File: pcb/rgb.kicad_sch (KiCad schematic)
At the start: 40 parts, among them J1 2.54-2*8P, J3 B4PS-VH, J4 TYPE-C-31-M-12, J5 TF-01A, J7 B4PS-VH, SW1 MS-22C01-G010, U4 EVQQ2, U5 ESP32-WROOM-32E, U7 CH340C, U8 SPX3819M5-L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

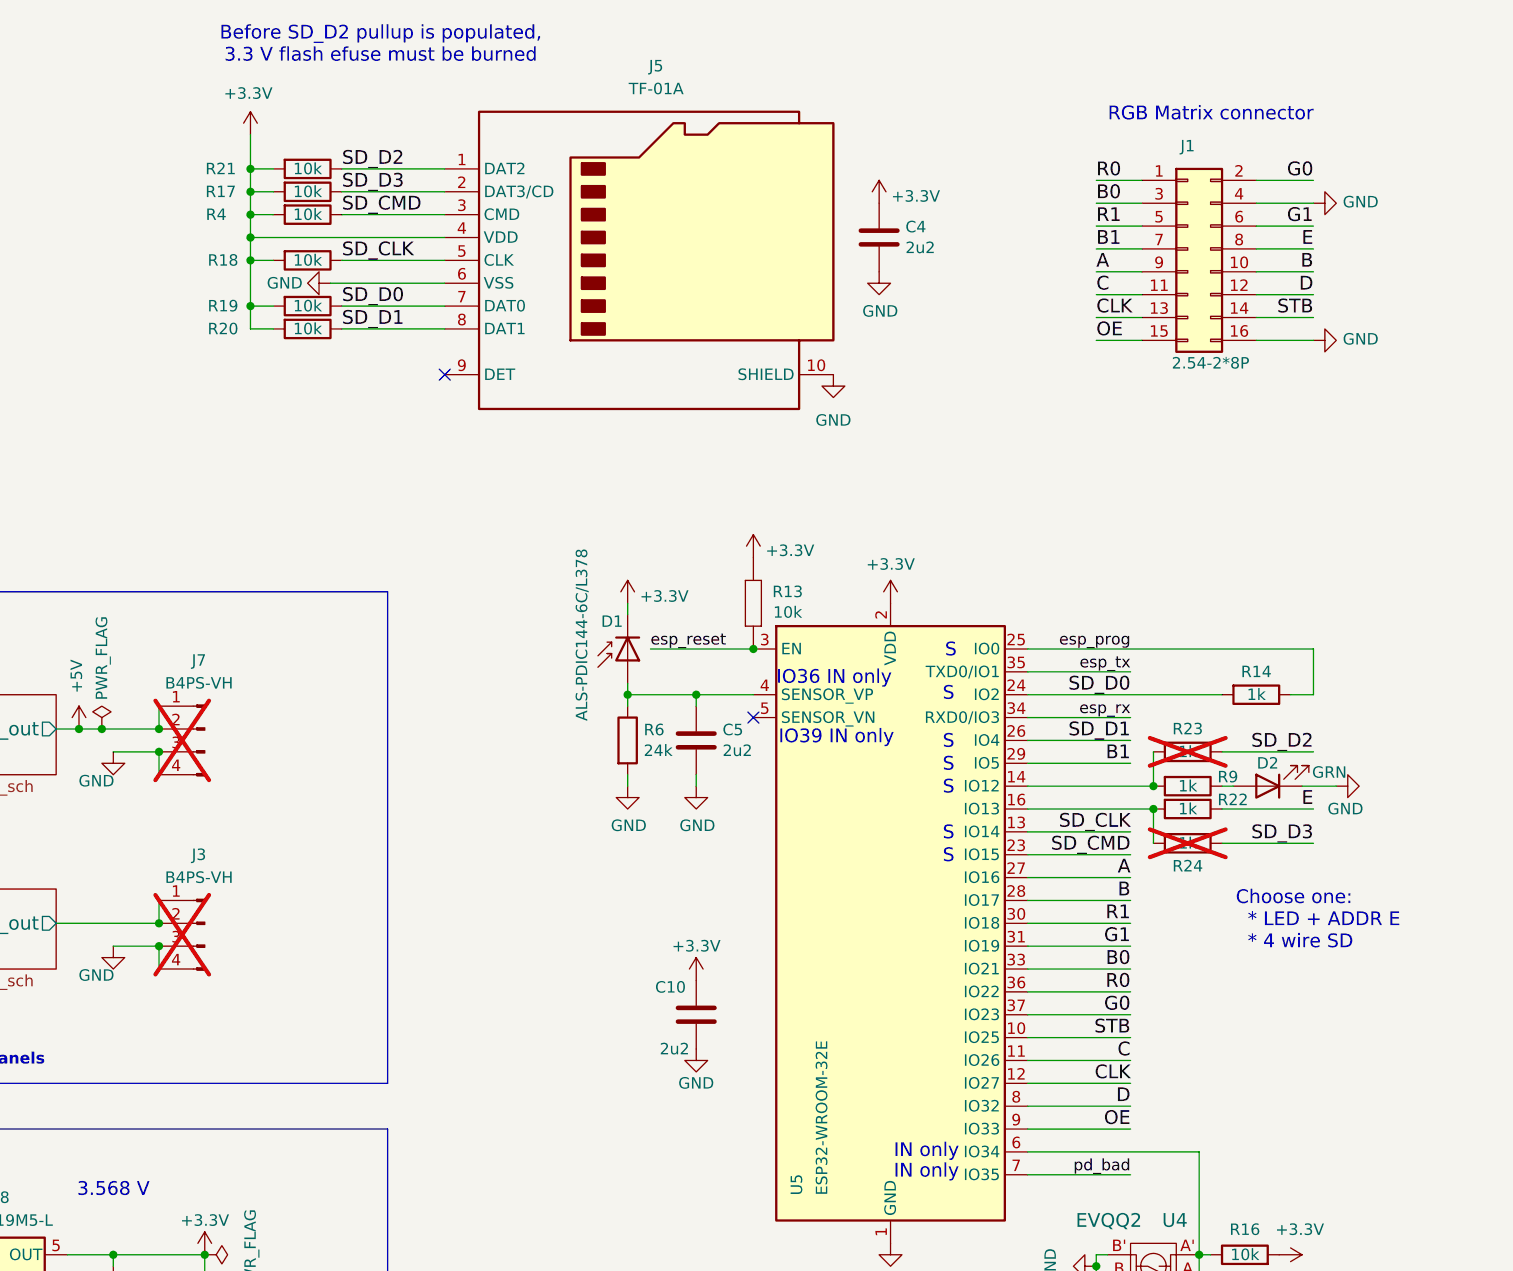
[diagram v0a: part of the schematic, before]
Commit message: sch: move comment
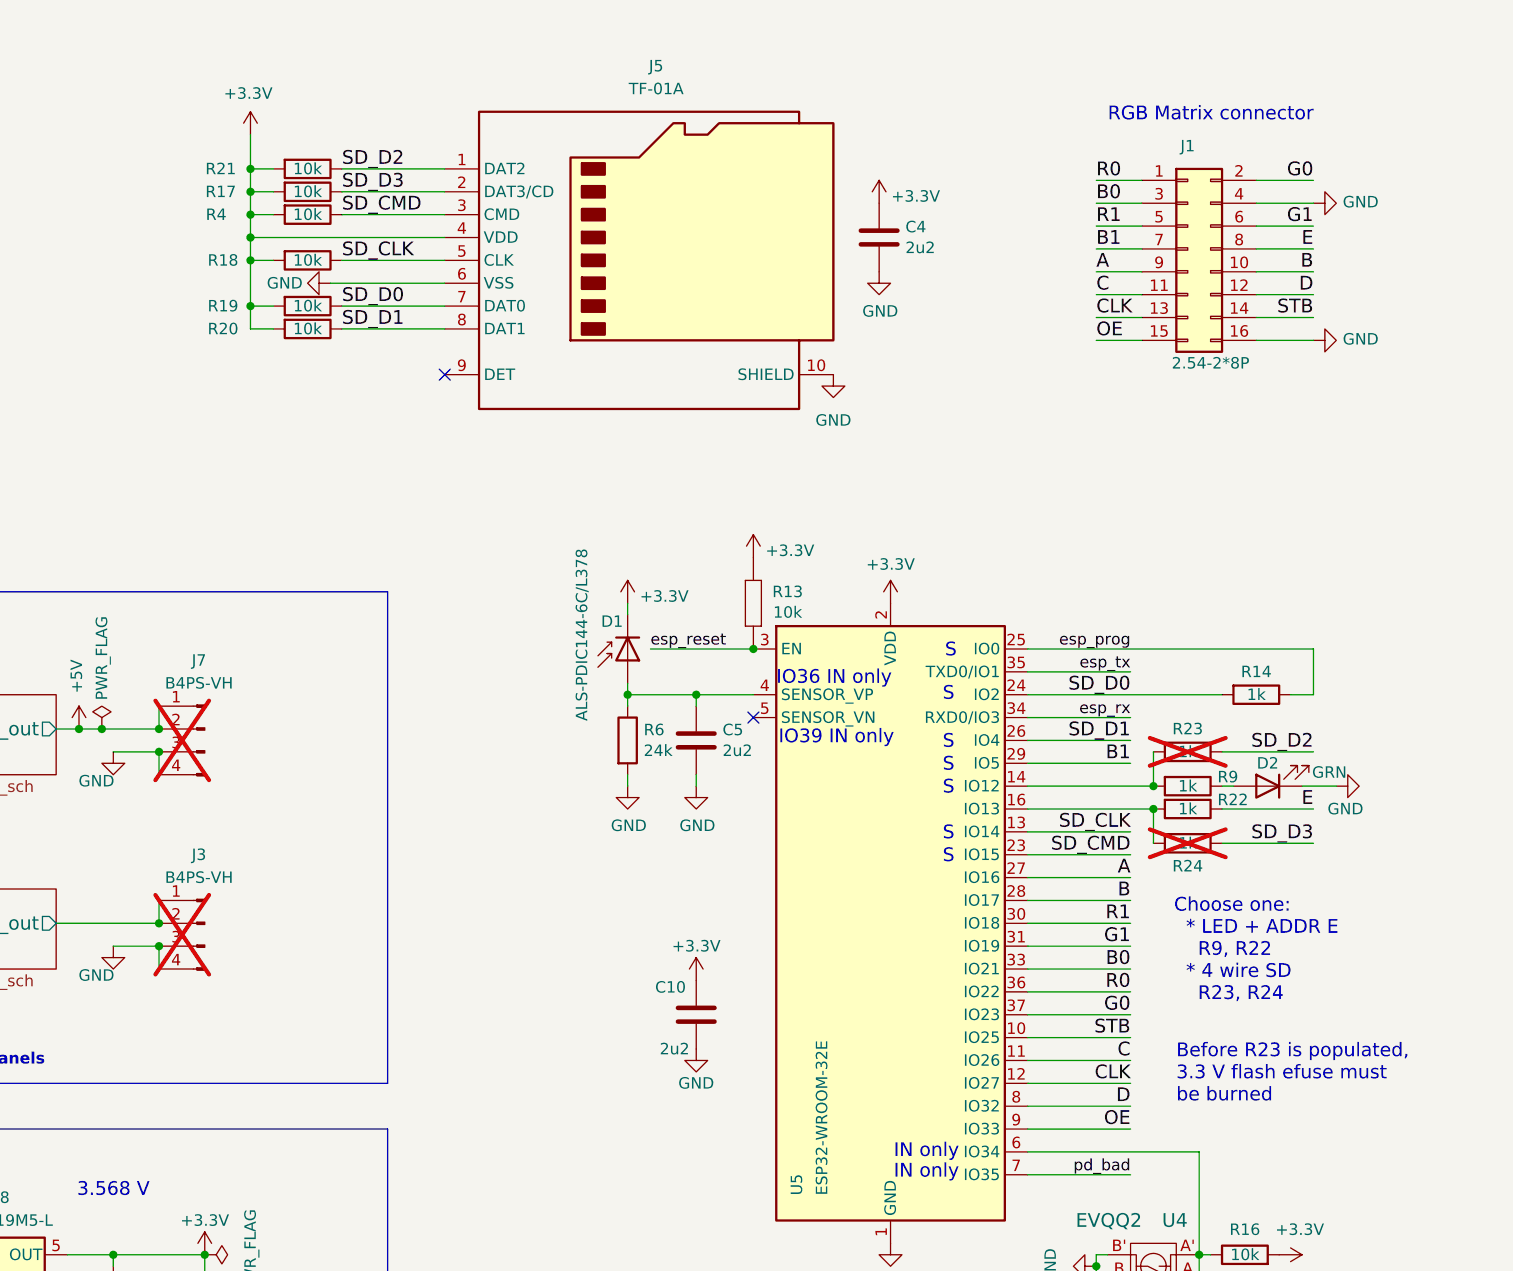
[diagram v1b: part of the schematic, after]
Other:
- note added: "Before R23 is populated, 3.3 V flash efuse must be burned"
- note added: "Choose one: * LED + ADDR E R9, R22 * 4 wire SD R23, R24"
- note removed: "Before SD_D2 pullup is populated, 3.3 V flash efuse must be burned"
- note removed: "Choose one: * LED + ADDR E * 4 wire SD"
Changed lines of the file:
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@@
 		)
 	)
-	(text "Choose one:\n  * LED + ADDR E\n  * 4 wire SD"
+	(text "Choose one:\n  * LED + ADDR E\n    R9, R22\n  * 4 wire SD\n    R23, R24"
 		(exclude_from_sim no)
-		(at 258.064 114.046 0)
+		(at 251.206 117.348 0)
 		(effects
 			(font
@@
 		)
 	)
-	(text "Before SD_D2 pullup is populated,\n3.3 V flash efuse must be burned"
+	(text "Before R23 is populated,\n3.3 V flash efuse must\nbe burned"
 		(exclude_from_sim no)
-		(at 163.068 16.764 0)
+		(at 251.46 131.064 0)
 		(effects
 			(font
 				(size 1.524 1.524)
 			)
+			(justify left)
 			(href "https://docs.espressif.com/projects/esp-idf/en/stable/esp32/api-reference/peripherals/sd_pullup_requirements.html#conflicts-between-bootstrap-and-sdio-on-dat2")
 		)

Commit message: do we have space fo the RTC?
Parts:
- added BT1: CR2032, Battery:BatteryHolder_Multicomp_BC-2001_1x2032, symbol Device:Battery_Cell
- added C30: 2u2, Capacitor_SMD:C_0603_1608Metric, symbol Device:C
- added R25, R26: 10k, Resistor_SMD:R_0603_1608Metric, symbol Device:R
- added U3: DS3232M, Package_SO:SOIC-8_3.9x4.9mm_P1.27mm, symbol Timer_RTC:DS3232M
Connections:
- net +3.3V: now also C30.1, R25.2, R26.2, U3.2 (VCC)
- net GND: now also BT1.2 (-), C30.2, U3.5 (GND)
- net SD_D2: no longer names the net of J5.1 (DAT2), R21.1
- net SD_D2: no longer R23.1
- net SD_D3: no longer names the net of J5.2 (DAT3/CD), R17.1
- net SD_D3: no longer R24.1
- new net: BT1.1 (+), U3.6 (VBAT)
- new net RTC_SCL: R23.1, R25.1, U3.8 (SCL)
- new net RTC_SDA: R24.1, R26.1, U3.7 (SDA)
- no-connect marks 12 -> 15
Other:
- note added: "Choose one: * LED + ADDR E R9, R22 * I2C RTC R23, R24"
- note removed: "Choose one: * LED + ADDR E R9, R22 * 4 wire SD R23, R24"

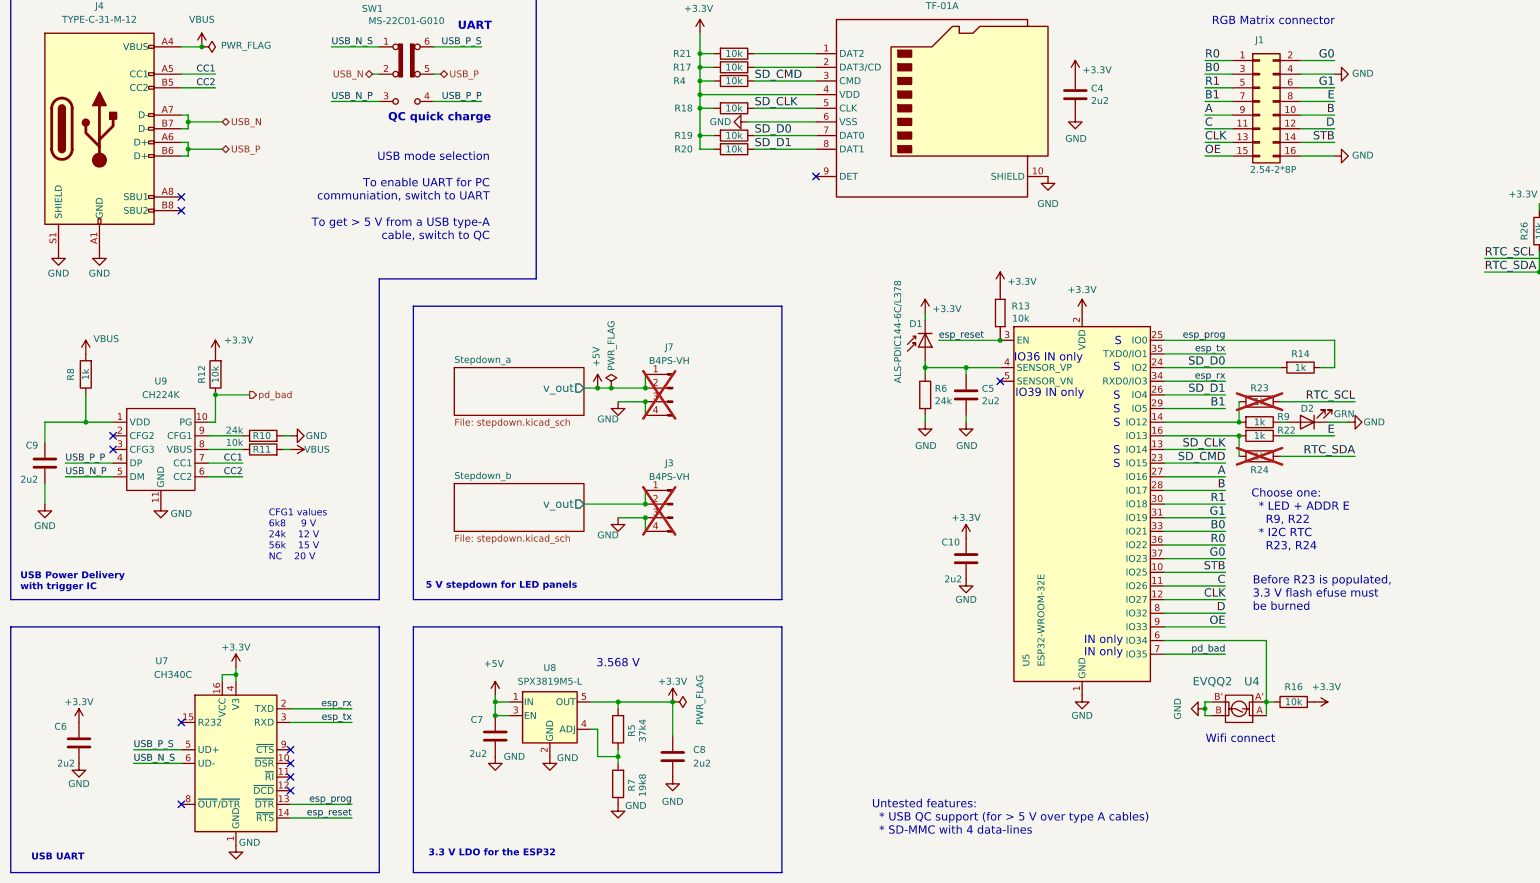
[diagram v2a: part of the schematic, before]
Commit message: pcb: add some items to the TODO list
  * detect 5 V operation with ADC
  * IR receiver
  * RTC chip
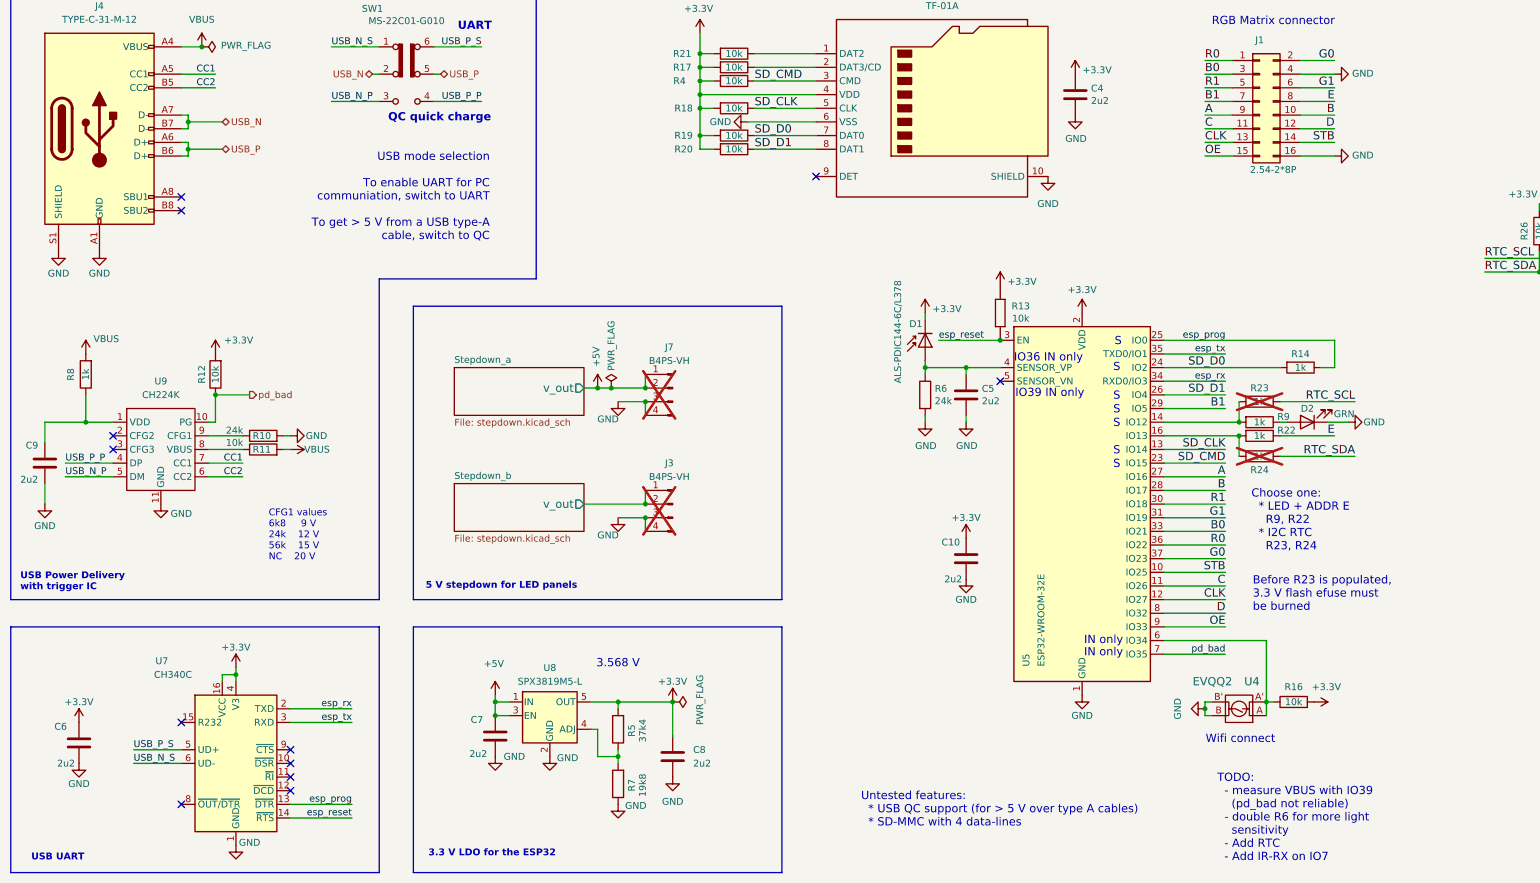
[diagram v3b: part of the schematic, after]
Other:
- note added: "TODO: - measure VBUS with IO39 (pd_bad not reliable) - double R6 for more light sensitivity - Add RTC - Add IR-RX on IO7"

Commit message: pcb: started to place components
looks like the Rev: 3 PCB will be the same size as Rev: 2
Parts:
- removed BT1: CR2032, Battery:BatteryHolder_Multicomp_BC-2001_1x2032, symbol Device:Battery_Cell
- removed C30: 2u2, Capacitor_SMD:C_0603_1608Metric, symbol Device:C
- removed R12, R26: 10k, Resistor_SMD:R_0603_1608Metric, symbol Device:R
- removed R13: 10k, Resistor_SMD:R_0603_1608Metric, symbol passive_resistors:R_0603_1%
- removed U3: DS3232M, Package_SO:SOIC-8_3.9x4.9mm_P1.27mm, symbol Timer_RTC:DS3232M
- added C31, C32: 2u2, Capacitor_SMD:C_0603_1608Metric, symbol Device:C
- added J6: V_BATT, Connector_PinHeader_2.54mm:PinHeader_1x02_P2.54mm_Vertical, symbol Connector:Conn_01x02_Pin
- added R27: 47k, Resistor_SMD:R_0603_1608Metric, symbol Device:R
- added R28: 220k, Resistor_SMD:R_0603_1608Metric, symbol Device:R
- added R53, R54: 10k, Resistor_SMD:R_0603_1608Metric, symbol Device:R
- added U11: RV-3028-C7, Package_SON:MicroCrystal_C7_SON-8_1.5x3.2mm_P0.9mm, symbol Timer_RTC:RV-3028-C7
- R6: value 24k -> 47k
- SW1: footprint (none) -> espirgbani:MS-22C01
- U9: symbol crtdriver2:CH224K -> espirgbani:CH224K
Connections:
- net +3.3V: now also C32.1, R53.2, R54.2, U11.7 (VDD)
- net GND: now also C31.2, C32.2, J6.2 (Pin_2), R27.2, U11.5 (VSS)
- net RTC_SCL: now also R54.1, U11.3 (SCL); no longer R25.1
- net RTC_SDA: now also R53.1, U11.4 (SDA)
- net VBUS: now also R28.1
- net esp_reset: now also R25.1
- net at U5.5 (SENSOR_VN): now also C31.1, R27.1, R28.2
- net pd_bad: no longer names the net of U9.10 (PG)
- net pd_bad: no longer U5.7 (IO35)
- new net: J6.1 (Pin_1), U11.6 (VBACKUP)
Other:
- note added: "- USB type A cable support (done) - SD-MMC with 2 data-lines (untested)"
- note added: "- measure VBUS with IO39 (done) - double R6 for > sensitivity (done) - Add RTC (done) - Add IR-receiver on IO7"
- note added: "3 V RTC battery backup voltage"
- note added: "5 V --> 0.881 V 9 V --> 1.584 V 12 V --> 2.112 V use ADC_ATTEN_DB_12"
- note added: "Swiss watch"
- note added: "to measure operating voltage"
- note removed: "TODO: - measure VBUS with IO39 (pd_bad not reliable) - double R6 for more light sensitivity - Add RTC - Add IR-RX on IO7"
- note removed: "Untested features: * USB QC support (for > 5 V over type A cables) * SD-MMC with 4 data-lines"
- moved on the sheet: C10, C4, C5, C6, C7, C8, C9, D1, D2, J1, J3, J4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
